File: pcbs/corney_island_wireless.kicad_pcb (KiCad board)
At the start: 2 copper layers, 133.8 x 91.7 mm, 96 parts

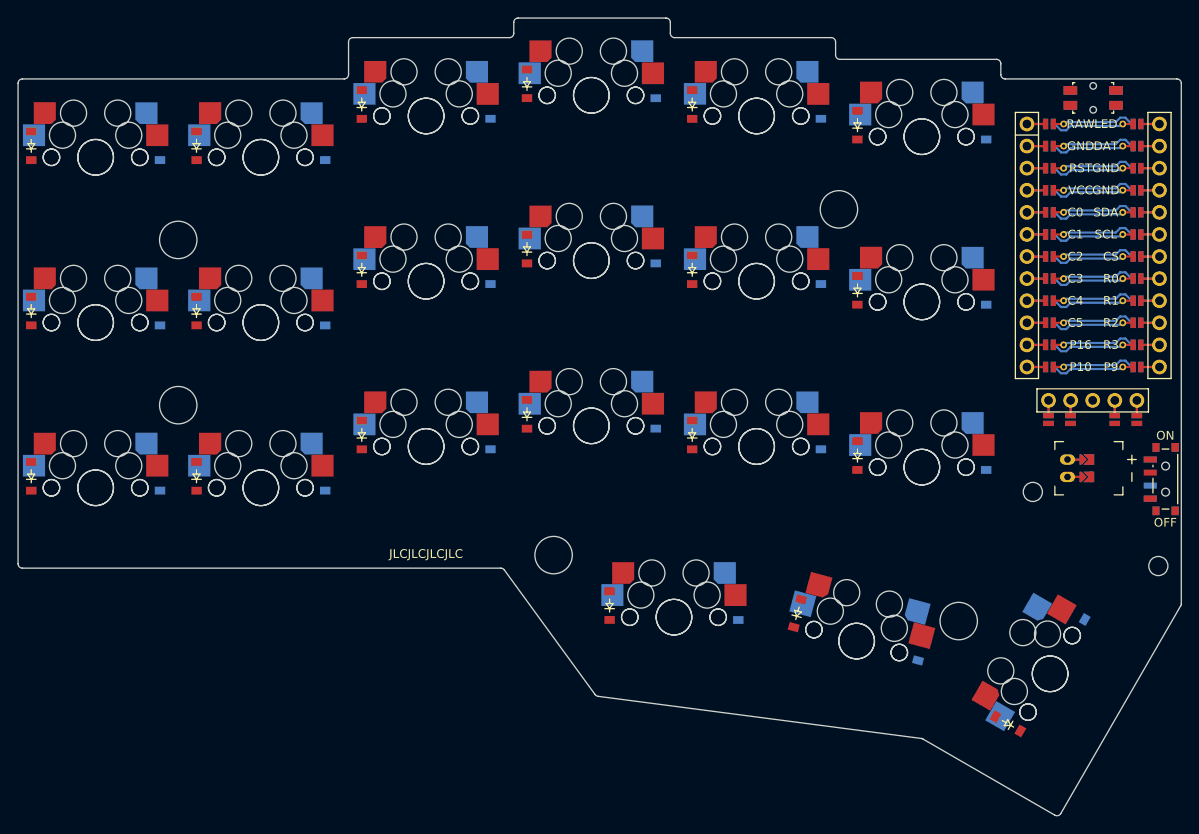
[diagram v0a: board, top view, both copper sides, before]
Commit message: build: regenerate outlines and PCBs using Ergogen v4.3.0
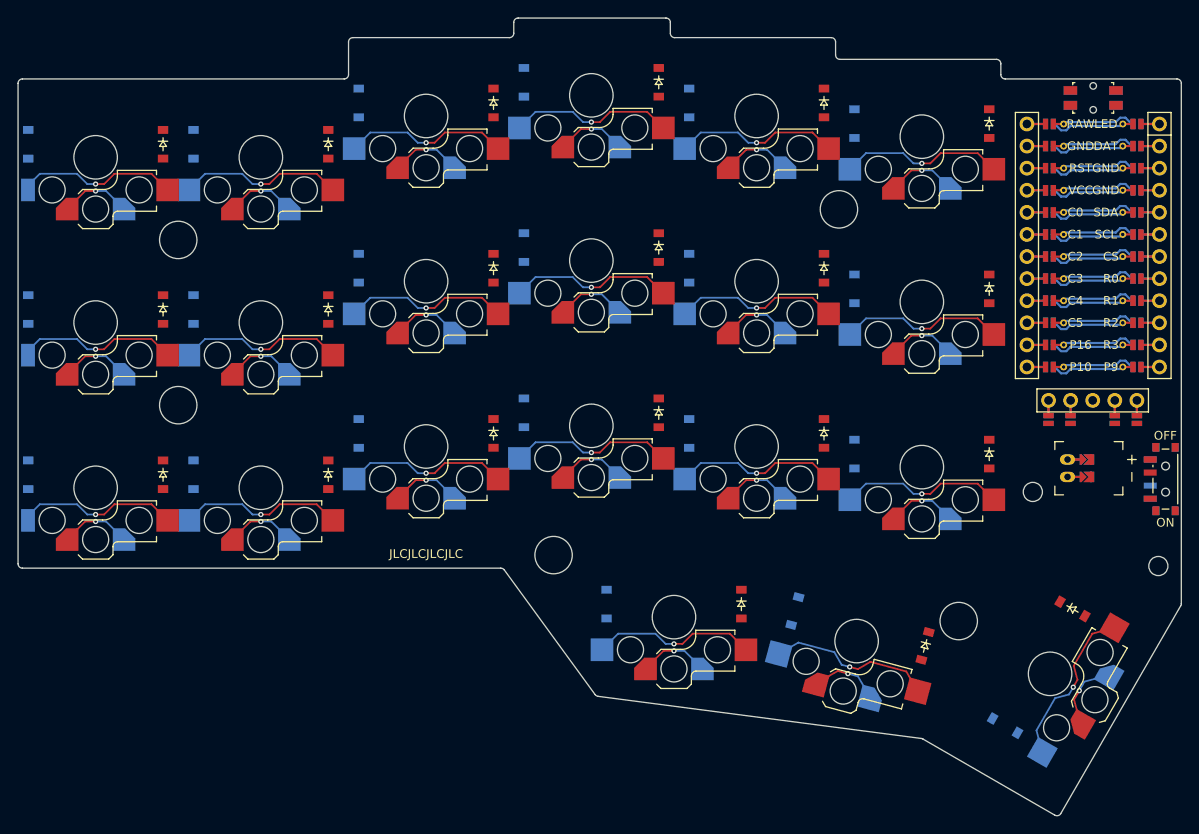
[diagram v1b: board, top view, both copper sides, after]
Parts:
- removed S22, S23, S24, S25, S26, S27, S28, S29, S30, S31, S32, S33, S34, S35, S36, S37, S38, S39, S40, S41, S42: , ceoloide:switch_mx
- S1, S10, S11, S12, S13, S14, S15, S16, S17, S18, S19, S2, S20, S21, S3, S4, S5, S6, S7, S8, S9: footprint ceoloide:switch_mx -> ceoloide:switch_choc_v1_v2
- moved D42 15.2 mm to (212.3, 113.9), turned to -30 degrees
- moved D41 15.2 mm to (195.4, 118.2), turned to -105 degrees
- moved D21 15.2 mm to (204.6, 127.4), turned to -30 degrees
- moved D1 15.2 mm to (92.2, 98.5), turned to -90 degrees
- moved D10 15.2 mm to (149.2, 91.4), turned to -90 degrees
- moved D11 15.2 mm to (149.2, 72.4), turned to -90 degrees
- moved D12 15.2 mm to (149.2, 53.4), turned to -90 degrees
- moved D13 15.2 mm to (168.2, 93.8), turned to -90 degrees
- moved D14 15.2 mm to (168.2, 74.8), turned to -90 degrees
- moved D15 15.2 mm to (168.2, 55.8), turned to -90 degrees
- moved D16 15.2 mm to (187.2, 96.1), turned to -90 degrees
- moved D17 15.2 mm to (187.2, 77.1), turned to -90 degrees
- moved D18 15.2 mm to (187.2, 58.1), turned to -90 degrees
- moved D19 15.2 mm to (158.8, 113.4), turned to -90 degrees
- moved D2 15.2 mm to (92.2, 79.5), turned to -90 degrees
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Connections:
- MCU1 pad 13: MCU1_12 -> MCU1_13
- MCU1 pad 14: MCU1_11 -> MCU1_14
- MCU1 pad 15: MCU1_10 -> MCU1_15
- MCU1 pad 16: MCU1_9 -> MCU1_16
- MCU1 pad 17: MCU1_8 -> MCU1_17
- MCU1 pad 18: MCU1_7 -> MCU1_18
- MCU1 pad 19: MCU1_6 -> MCU1_19
- MCU1 pad 20: MCU1_5 -> MCU1_20
- MCU1 pad 21: MCU1_4 -> MCU1_21
- MCU1 pad 22: MCU1_3 -> MCU1_22
- MCU1 pad 23: MCU1_2 -> MCU1_23
- MCU1 pad 24: MCU1_1 -> MCU1_24
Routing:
- net C5: track 0.00 -> 33.1 mm, vias 0 -> 4
- net C4: track 0.00 -> 33.1 mm, vias 0 -> 4
- net C3: track 0.00 -> 33.1 mm, vias 0 -> 4
- net C1: track 0.00 -> 24.8 mm, vias 0 -> 3
- net C0: track 0.00 -> 24.8 mm, vias 0 -> 3
- net C2: track 0.00 -> 24.8 mm, vias 0 -> 3
- net pinky_top_B: track 0.00 -> 19.1 mm, vias 0 -> 1
- net pinky_home_B: track 0.00 -> 19.1 mm, vias 0 -> 1
- net pinky_bottom_B: track 0.00 -> 19.1 mm, vias 0 -> 1
- net outer_top_B: track 0.00 -> 19.1 mm, vias 0 -> 1
- net outer_home_B: track 0.00 -> 19.1 mm, vias 0 -> 1
- net outer_bottom_B: track 0.00 -> 19.1 mm, vias 0 -> 1
- net ring_top_B: track 0.00 -> 19.1 mm, vias 0 -> 1
- net ring_home_B: track 0.00 -> 19.1 mm, vias 0 -> 1
- net ring_bottom_B: track 0.00 -> 19.1 mm, vias 0 -> 1
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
